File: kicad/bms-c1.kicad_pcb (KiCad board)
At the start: 4 copper layers, 135 x 70 mm, 210 parts, among them J1 MicroFit 2x12, J2 B4B-PH-SM4, J3 USB_B_Micro, J4 B3B-PH-SM4, J5 B2B-PH-SM4, J6 B4B-PH-SM4, P1 CONN_01X01, P2 CONN_01X01, P3 CONN_01X01, P4 CONN_01X01, P5 CONN_01X01, Q1 DMN10H220LE, Q10 BSS84, Q11 BSS123N, Q12 ZXMP10A17GTA, Q13 BSS123N, Q2 IPT015N10N5, Q3 IPT015N10N5, Q4 IPT015N10N5, Q5 IPT015N10N5, Q6 IPT015N10N5, Q7 IPT015N10N5, Q8 IPT015N10N5, Q9 IPT015N10N5, U2 LMR16030, U3 SN65HVD230, U4 BQ76952, U5 ESP32-C3-MINI-1

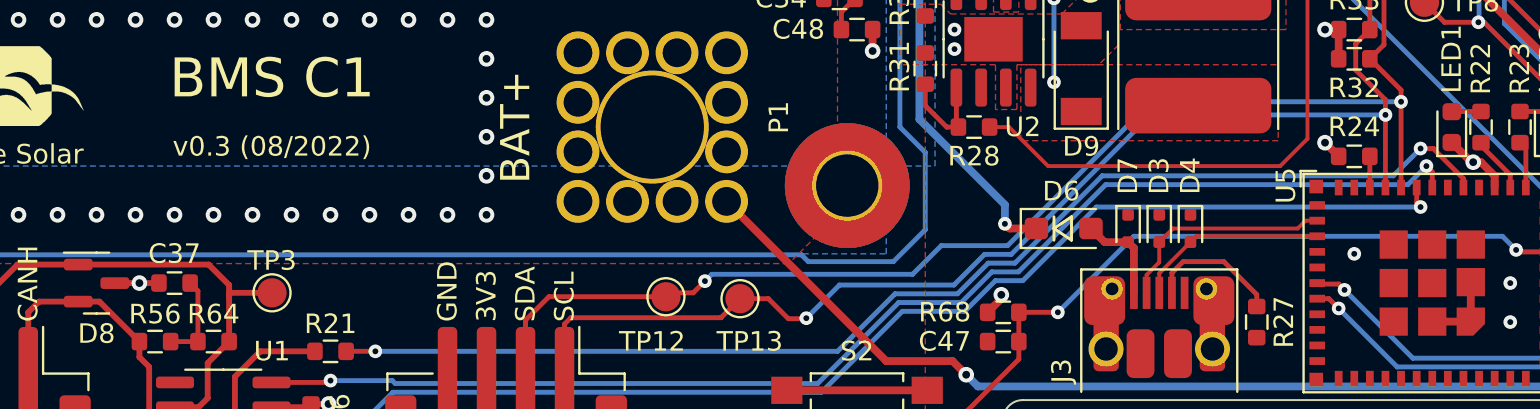
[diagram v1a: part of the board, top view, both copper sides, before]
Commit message: Board v0.3.1: Add test point for GPIO9 (BOOT) pin
Fixes #34
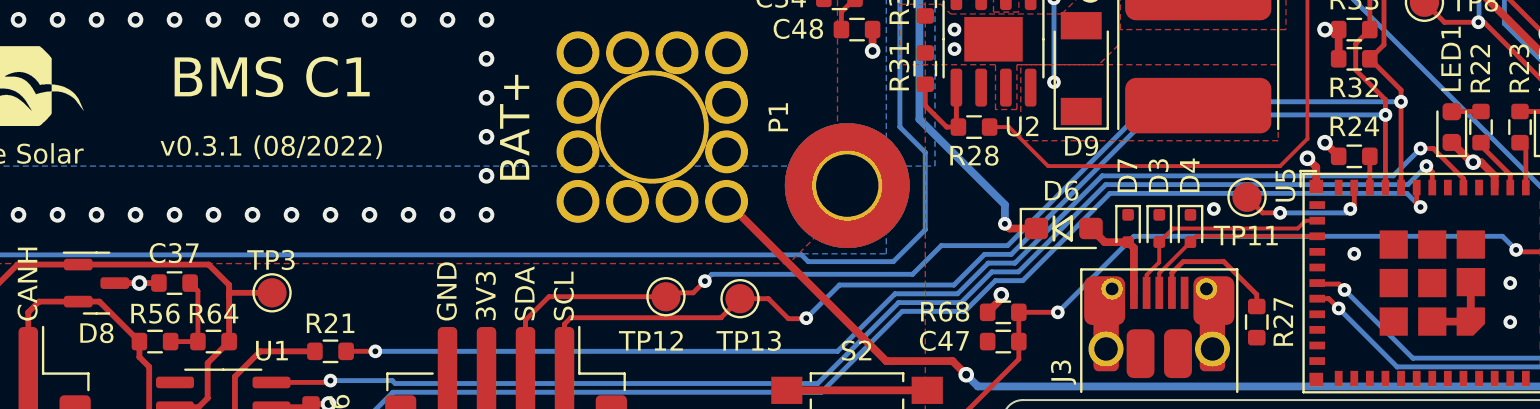
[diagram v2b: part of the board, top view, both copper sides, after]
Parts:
- added TP11: TestPoint, TestPoint:TestPoint_Pad_D1.5mm, F.Cu at (160.5, 104.6)
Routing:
- net /ESP32-C3 MCU/BOOT: track 0.00 -> 6.90 mm, vias 0 -> 2
- net GND: track 66.3 -> 67.9 mm, vias 43 -> 45
- net /ESP32-C3 MCU/CAN_TX: track 65.7 -> 66.3 mm
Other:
- board text added: "v0.3.1 (08/2022)"
- board text removed: "v0.3 (08/2022)"

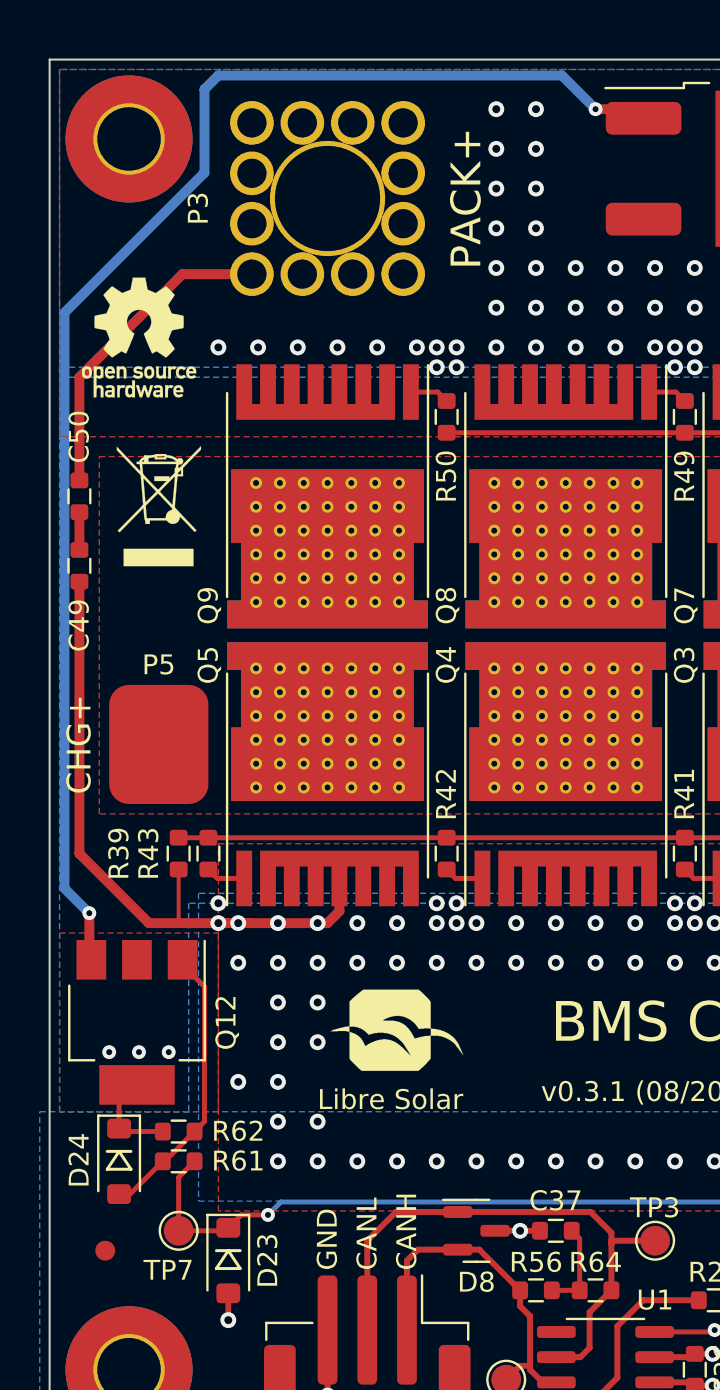
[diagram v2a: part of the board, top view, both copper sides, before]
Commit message: Swap D and S of Q12
Fixes #36
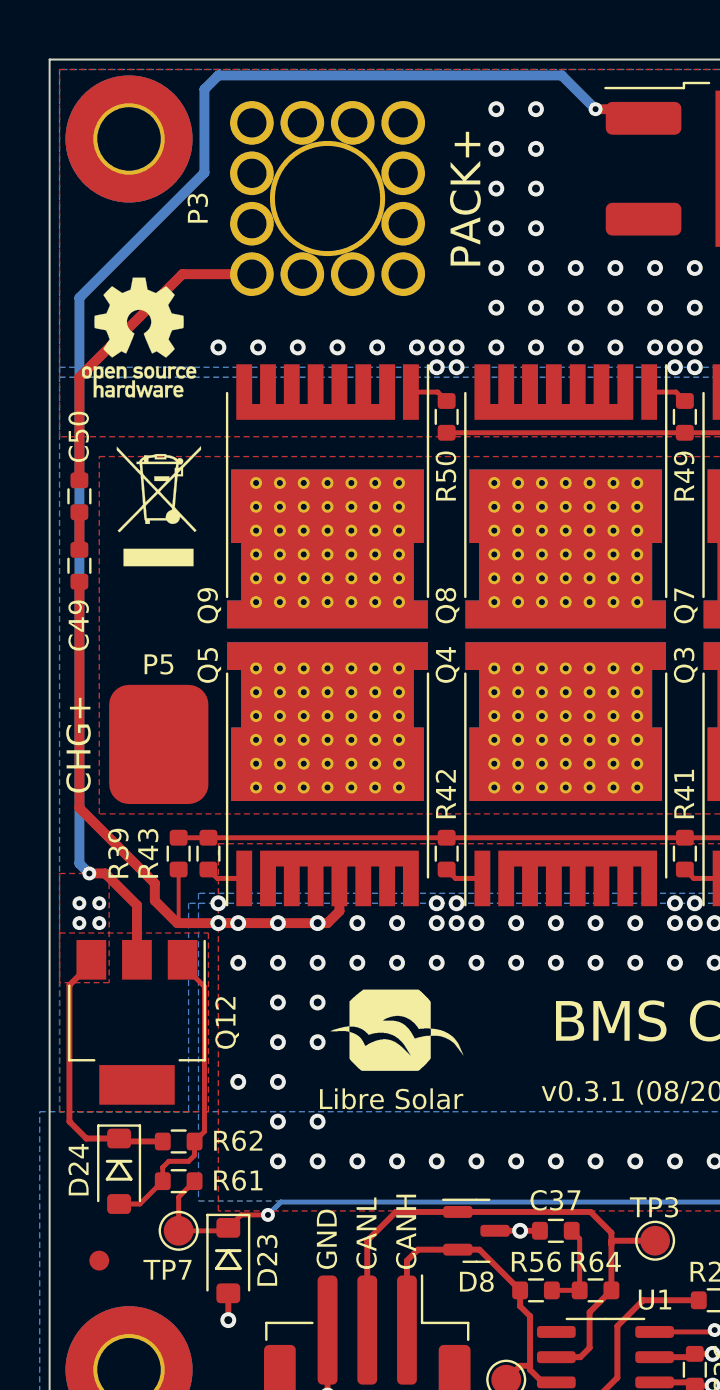
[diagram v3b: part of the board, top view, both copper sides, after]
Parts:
- moved R61 1.00 mm to (86.5, 106.5)
- moved FID1 0.58 mm to (82.5, 110.5)
- moved D24 0.50 mm to (83.5, 106.0)
- moved R62 0.50 mm to (86.5, 104.5)
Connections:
- net /ESP32-C3 MCU/EN renamed /ESP32-C3 MCU/NRST
- Q12 pad 2: /CHG+ -> Net-(Q12-Pad2)
- Q12 pad 3: Net-(Q12-Pad3) -> /CHG+
- R63 pad 1: Net-(Q12-Pad3) -> Net-(Q12-Pad2)
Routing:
- net Net-(Q12-Pad2): track 0.00 -> 71.4 mm, vias 0 -> 2
- net Net-(Q12-Pad3): track 70.6 -> 0.00 mm, vias 2 -> 0
- net /CHG+: track 4.83 -> 13.9 mm, vias 3 -> 4
- net Net-(D24-Pad2): track 14.4 -> 15.7 mm
- net /BQ76952/PDSG: track 105.5 -> 104.5 mm
- net /BAT+: track 153.9 -> 153.0 mm
- added copper zone on F.Cu, net Net-(Q12-Pad2)

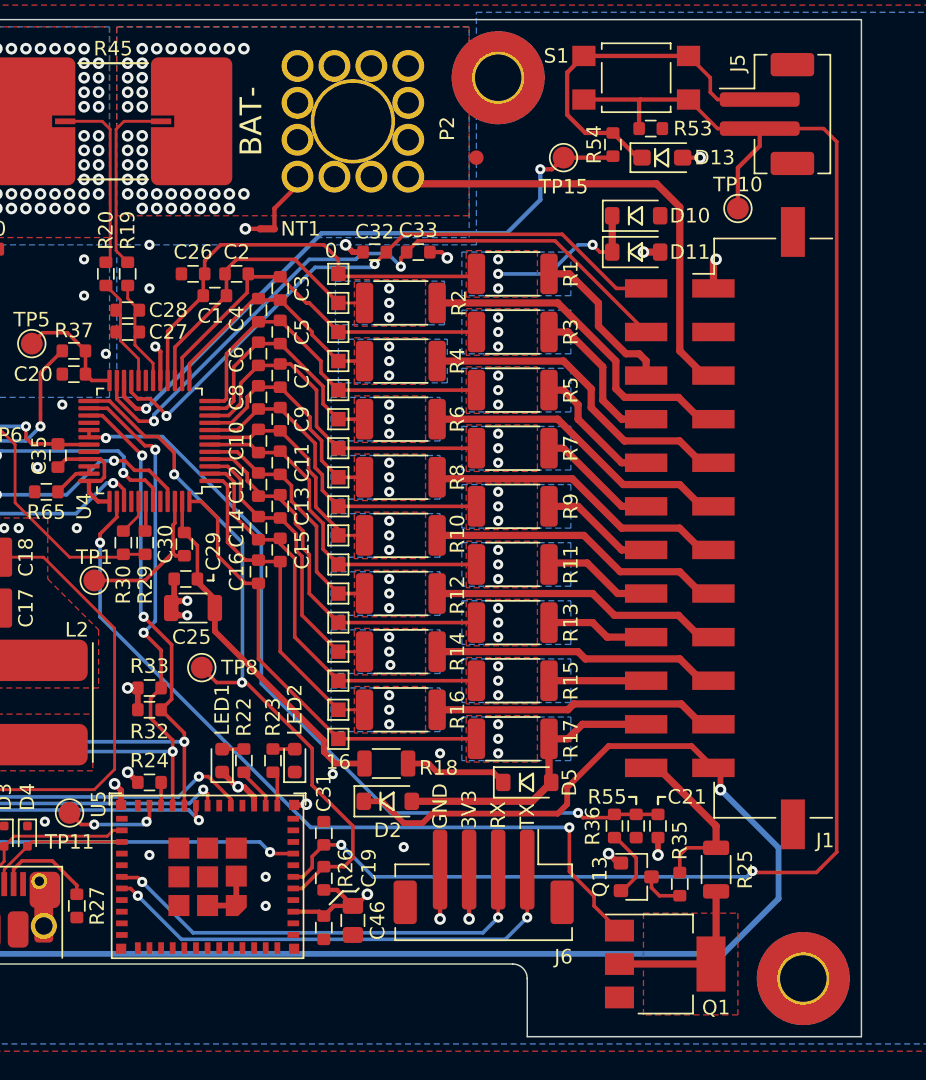
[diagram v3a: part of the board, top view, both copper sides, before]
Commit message: Remove FUSE_DETECT circuit
Q13 was not properly tied to ground, so it was not switching on the
voltage divider. A voltage divider that is continuously on would
draw current even in deepsleep mode, so it is not viable for a BMS.

I could not come up with an easy circuit that allows monitoring the
voltage without any power consumption, so the fuse diagnosis
mechanism is removed for now.
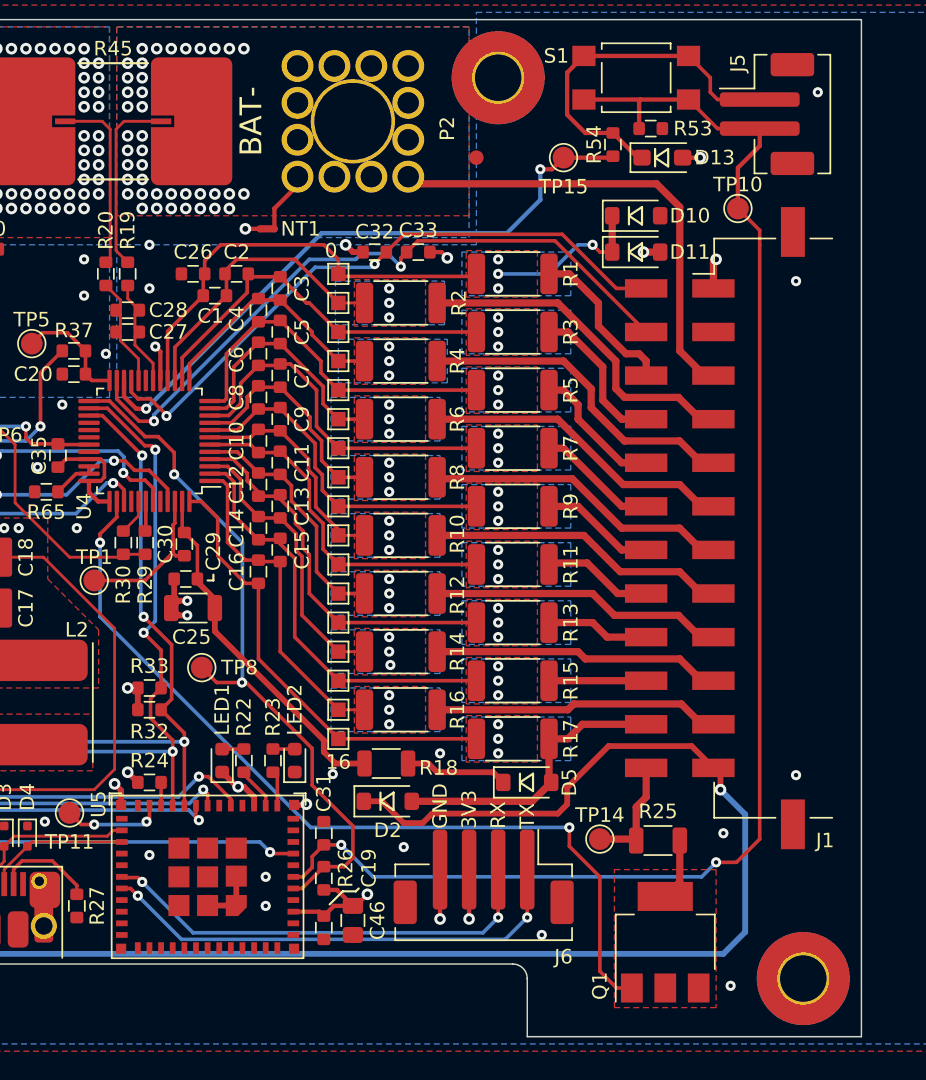
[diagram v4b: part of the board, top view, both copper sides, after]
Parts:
- removed C21: 100nF, LibreSolar:C_0603_1608
- removed Q13: BSS123N, LibreSolar:SOT-23
- removed R35: 1M, LibreSolar:R_0603_1608
- removed R36, R55: 100k, LibreSolar:R_0603_1608
- added TP14: TestPoint, TestPoint:TestPoint_Pad_D1.5mm, F.Cu at (197.0, 106.4)
- moved R25 4.47 mm to (201.0, 106.5), turned to 180 degrees
- moved Q1 1.50 mm to (201.5, 113.5), turned to 90 degrees
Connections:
- U4 pad 29: /BQ76952/FUSE_DETECT -> unconnected-(U4-Pad29)
- U4 pad 30: /BQ76952/FUSE_DETECT -> unconnected-(U4-Pad30)
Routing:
- net /BQ76952/FUSE_DETECT: track 56.7 -> 0.00 mm, vias 2 -> 0
- net /BTN_LOW: track 116.1 -> 100.6 mm
- net Net-(Q1-Pad2): track 11.4 -> 4.26 mm
- net Net-(U4-Pad38): track 55.3 -> 60.2 mm
- net Net-(Q13-Pad2): track 4.72 -> 0.00 mm
- net /FUSE: track 11.9 -> 7.83 mm
- net Net-(Q13-Pad3): track 2.93 -> 0.00 mm
- net /BAT+: track 153.0 -> 151.1 mm
- net +3V3: track 62.0 -> 60.8 mm, vias 11 -> 10
- net GND: track 67.9 -> 66.7 mm, vias 45 -> 50
